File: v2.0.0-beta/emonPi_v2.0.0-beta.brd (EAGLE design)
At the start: 91.4 x 138.4 mm, 79 parts, among them IC1 AVR128DB32-I_PT, IC2 MCP1501-10E_SN, J1 SJ-3524-SMT-TR, J2 SJ-3524-SMT-TR, J4 SJ-3524-SMT-TR, J9 RJ11, Y1 MCSJK-7U-12.00-12-10-80-B-10

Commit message: updated board file
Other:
- board size 91.4 x 138.4 mm -> 85 x 88 mm

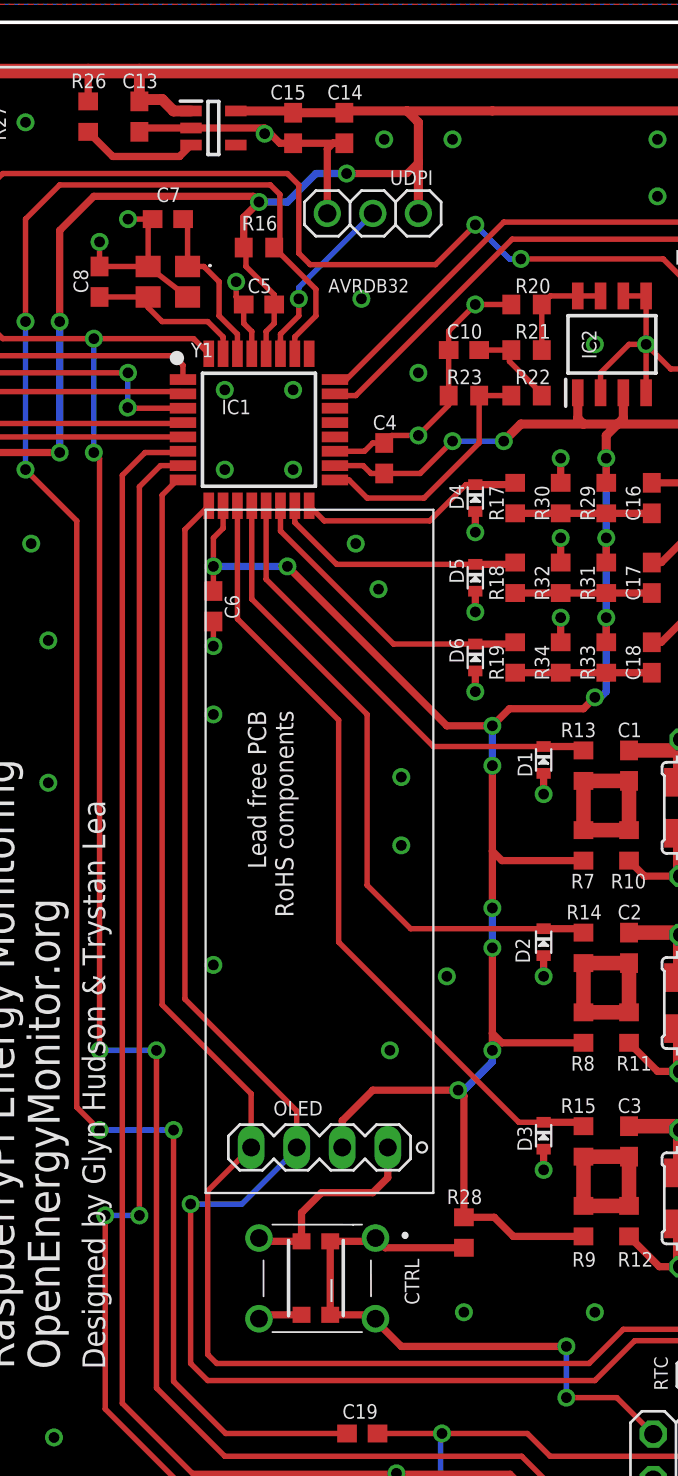
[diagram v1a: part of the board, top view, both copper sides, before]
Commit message: fix push switch
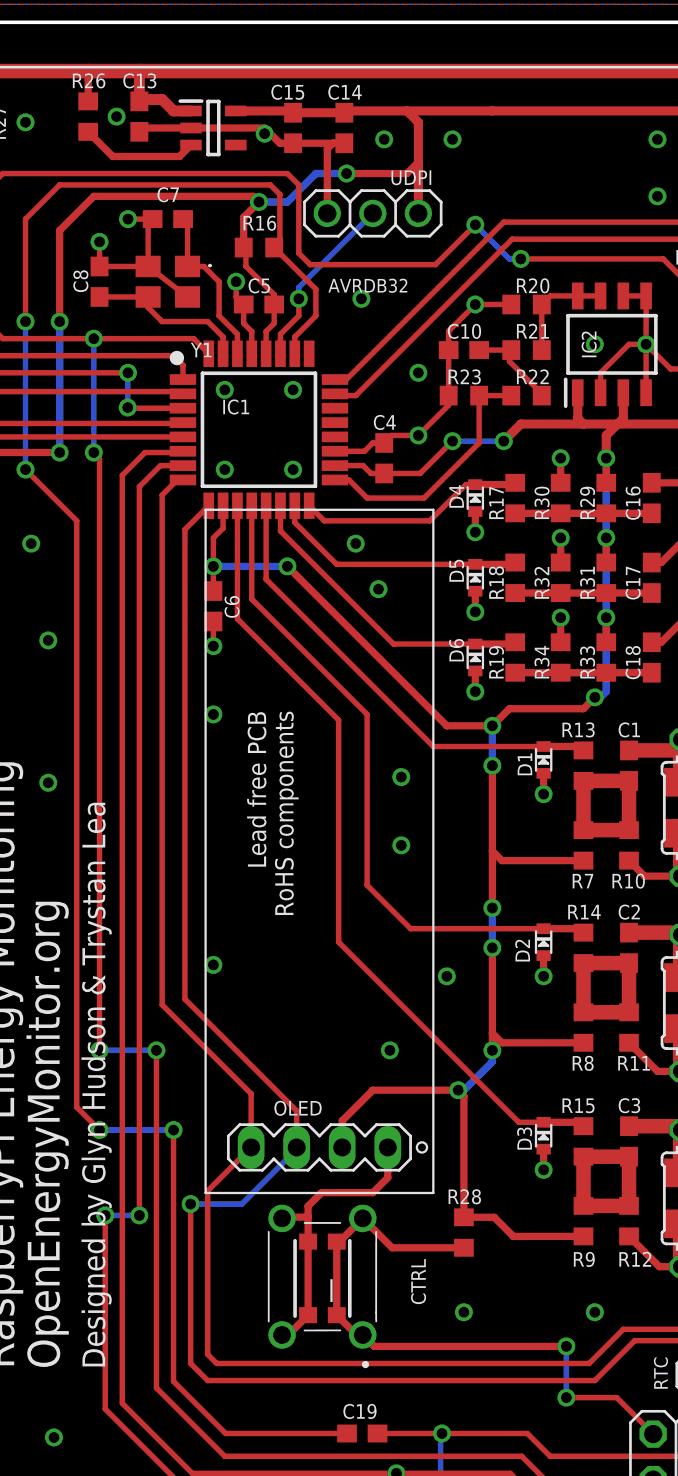
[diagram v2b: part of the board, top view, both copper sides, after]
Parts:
- moved S1 0.44 mm to (50.5, 15.6), turned to 270 degrees
- moved CTRL 0.37 mm to (50.5, 16.0)
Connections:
- net CONTROL: now also S1.3; no longer S1.2
- net GND: now also S1.2; no longer S1.3
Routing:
- net GND: track 185.2 -> 187.6 mm, vias 57 -> 58
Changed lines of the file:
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@@
 <attribute name="NAME" x="47.7455" y="25.033" size="0.8128" layer="25" font="vector" ratio="20"/>
 </element>
-<element name="CTRL" library="microbuilder" package="BTN_KMR2_4.6X2.8" value="KMR2" x="50.1175" y="15.97" smashed="yes" rot="R270">
-<attribute name="NAME" x="55.0705" y="17.0495" size="0.8128" layer="25" font="vector" ratio="20" rot="R270"/>
+<element name="CTRL" library="microbuilder" package="BTN_KMR2_4.6X2.8" value="KMR2" x="50.4825" y="15.9512" smashed="yes" rot="R270">
+<attribute name="NAME" x="55.4355" y="17.0307" size="0.8128" layer="25" font="vector" ratio="20" rot="R270"/>
 </element>
 <element name="R28" library="rcl" package="R0603" value="10K" x="58.3725" y="18.51" smashed="yes" rot="R270">
@@
 <attribute name="VALUE" x="82.9" y="10.445" size="1.27" layer="27" rot="R180"/>
 </element>
-<element name="S1" library="2-1825910-7" package="218259107" value="2-1825910-7" x="50.6825" y="15.9525" smashed="yes">
-<attribute name="ARROW_PART_NUMBER" value="2-1825910-7" x="50.6825" y="15.9525" size="0.8128" layer="27" font="vector" ratio="20" display="off"/>
-<attribute name="ARROW_PRICE-STOCK" value="https://www.arrow.com/en/products/2-1825910-7/te-connectivity?region=europe" x="50.6825" y="15.9525" size="0.8128" layer="27" font="vector" ratio="20" display="off"/>
-<attribute name="DESCRIPTION" value="Relays, Contactors &amp; Switches   Switches   Tactile Switches FSM14JH=6MM TACT SWITCH, HIGH TEMP" x="50.6825" y="15.9525" size="0.8128" layer="27" font="vector" ratio="20" display="off"/>
-<attribute name="HEIGHT" value="13mm" x="50.6825" y="15.9525" size="0.8128" layer="27" font="vector" ratio="20" display="off"/>
-<attribute name="MANUFACTURER_NAME" value="TE Connectivity" x="50.6825" y="15.9525" size="0.8128" layer="27" font="vector" ratio="20" display="off"/>
-<attribute name="MANUFACTURER_PART_NUMBER" value="2-1825910-7" x="50.6825" y="15.9525" size="0.8128" layer="27" font="vector" ratio="20" display="off"/>
-<attribute name="MOUSER_PART_NUMBER" value="506-2-1825910-7" x="50.6825" y="15.9525" size="0.8128" layer="27" font="vector" ratio="20" display="off"/>
-<attribute name="MOUSER_PRICE-STOCK" value="https://www.mouser.co.uk/ProductDetail/TE-Connectivity-PB/2-1825910-7?qs=epcAG6di8szpGFLvuwXKeQ%3D%3D" x="50.6825" y="15.9525" size="0.8128" layer="27" font="vector" ratio="20" display="off"/>
+<element name="S1" library="2-1825910-7" package="218259107" value="2-1825910-7" x="50.4825" y="15.5575" smashed="yes" rot="R270">
+<attribute name="ARROW_PART_NUMBER" value="2-1825910-7" x="50.4825" y="15.5575" size="0.8128" layer="27" font="vector" ratio="20" rot="R270" display="off"/>
+<attribute name="ARROW_PRICE-STOCK" value="https://www.arrow.com/en/products/2-1825910-7/te-connectivity?region=europe" x="50.4825" y="15.5575" size="0.8128" layer="27" font="vector" ratio="20" rot="R270" display="off"/>
+<attribute name="DESCRIPTION" value="Relays, Contactors &amp; Switches   Switches   Tactile Switches FSM14JH=6MM TACT SWITCH, HIGH TEMP" x="50.4825" y="15.5575" size="0.8128" layer="27" font="vector" ratio="20" rot="R270" display="off"/>
+<attribute name="HEIGHT" value="13mm" x="50.4825" y="15.5575" size="0.8128" layer="27" font="vector" ratio="20" rot="R270" display="off"/>
+<attribute name="MANUFACTURER_NAME" value="TE Connectivity" x="50.4825" y="15.5575" size="0.8128" layer="27" font="vector" ratio="20" rot="R270" display="off"/>
+<attribute name="MANUFACTURER_PART_NUMBER" value="2-1825910-7" x="50.4825" y="15.5575" size="0.8128" layer="27" font="vector" ratio="20" rot="R270" display="off"/>
+<attribute name="MOUSER_PART_NUMBER" value="506-2-1825910-7" x="50.4825" y="15.5575" size="0.8128" layer="27" font="vector" ratio="20" rot="R270" display="off"/>
+<attribute name="MOUSER_PRICE-STOCK" value="https://www.mouser.co.uk/ProductDetail/TE-Connectivity-PB/2-1825910-7?qs=epcAG6di8szpGFLvuwXKeQ%3D%3D" x="50.4825" y="15.5575" size="0.8128" layer="27" font="vector" ratio="20" rot="R270" display="off"/>
 </element>
 <element name="JP3" library="SparkFun" package="FTDI_BASIC" value="6x1" x="57.07" y="2.27" smashed="yes" rot="R180"/>
@@
 <vertex x="3" y="-4"/>
 </polygon>
-<contactref element="S1" pad="3"/>
-<contactref element="S1" pad="4"/>
-<wire x1="49.3175" y1="18.02" x2="47.125" y2="18.02" width="0.4064" layer="1"/>
-<wire x1="47.125" y1="18.02" x2="46.9425" y2="18.2025" width="0.4064" layer="1"/>
-<wire x1="49.3175" y1="13.92" x2="47.16" y2="13.92" width="0.4064" layer="1"/>
-<wire x1="47.16" y1="13.92" x2="46.9425" y2="13.7025" width="0.4064" layer="1"/>
-<wire x1="49.3175" y1="18.02" x2="49.3175" y2="19.615" width="0.4064" layer="1"/>
 <wire x1="54.1275" y1="21.5675" x2="54.1275" y2="23.255" width="0.4064" layer="1"/>
-<wire x1="49.3175" y1="19.615" x2="50.435" y2="20.7325" width="0.4064" layer="1"/>
 <wire x1="50.435" y1="20.7325" x2="53.2925" y2="20.7325" width="0.4064" layer="1"/>
 <wire x1="53.2925" y1="20.7325" x2="54.1275" y2="21.5675" width="0.4064" layer="1"/>
@@
 <contactref element="JP3" pad="GND"/>
 <contactref element="JP2" pad="5"/>
+<contactref element="S1" pad="4"/>
+<contactref element="S1" pad="2"/>
+<wire x1="49.6825" y1="18.0012" x2="49.6825" y2="19.3675" width="0.4064" layer="1"/>
+<wire x1="49.6825" y1="19.3675" x2="49.6825" y2="19.98" width="0.4064" layer="1"/>
+<wire x1="49.6825" y1="19.98" x2="50.435" y2="20.7325" width="0.4064" layer="1"/>
+<wire x1="48.2325" y1="19.2975" x2="48.3025" y2="19.3675" width="0.4064" layer="1"/>
+<wire x1="48.3025" y1="19.3675" x2="49.6825" y2="19.3675" width="0.4064" layer="1"/>
+<wire x1="48.2325" y1="12.7975" x2="48.5788" y2="12.7975" width="0.4064" layer="1"/>
+<wire x1="48.5788" y1="12.7975" x2="49.6825" y2="13.9012" width="0.4064" layer="1"/>
+<wire x1="49.6825" y1="18.0012" x2="49.6825" y2="13.9012" width="0.4064" layer="1"/>
+<via x="39.005" y="80.74" extent="1-16" drill="0.6"/>
 </signal>
 <signal name="3.3V">
@@
 <wire x1="66.8975" y1="9.3025" x2="64.0875" y2="9.3025" width="0.3048" layer="1"/>
 <contactref element="JP1" pad="11"/>
+<contactref element="S1" pad="3"/>
 <contactref element="S1" pad="1"/>
-<contactref element="S1" pad="2"/>
-<wire x1="50.9175" y1="18.02" x2="53.26" y2="18.02" width="0.4064" layer="1"/>
-<wire x1="53.26" y1="18.02" x2="53.4425" y2="18.2025" width="0.4064" layer="1"/>
-<wire x1="50.9175" y1="13.92" x2="53.225" y2="13.92" width="0.4064" layer="1"/>
-<wire x1="53.225" y1="13.92" x2="53.4425" y2="13.7025" width="0.4064" layer="1"/>
-<wire x1="53.4425" y1="18.2025" x2="53.985" y2="17.66" width="0.4064" layer="1"/>
-<wire x1="53.985" y1="17.66" x2="58.3725" y2="17.66" width="0.4064" layer="1"/>
-<wire x1="64.0875" y1="12.16" x2="54.88" y2="12.16" width="0.4064" layer="1"/>
-<wire x1="54.88" y1="12.16" x2="53.4425" y2="13.5975" width="0.4064" layer="1"/>
-<wire x1="53.4425" y1="13.5975" x2="53.4425" y2="13.7025" width="0.4064" layer="1"/>
-<wire x1="50.9175" y1="18.02" x2="50.9175" y2="13.92" width="0.4064" layer="1"/>
+<wire x1="52.7325" y1="19.2975" x2="51.4362" y2="18.0012" width="0.4064" layer="1"/>
+<wire x1="51.4362" y1="18.0012" x2="51.2825" y2="18.0012" width="0.4064" layer="1"/>
+<wire x1="58.3725" y1="17.66" x2="54.37" y2="17.66" width="0.4064" layer="1"/>
+<wire x1="54.37" y1="17.66" x2="52.7325" y2="19.2975" width="0.4064" layer="1"/>
+<wire x1="51.2825" y1="18.0012" x2="51.2825" y2="13.9012" width="0.4064" layer="1"/>
+<wire x1="51.2825" y1="13.9012" x2="52.3862" y2="12.7975" width="0.4064" layer="1"/>
+<wire x1="52.3862" y1="12.7975" x2="52.7325" y2="12.7975" width="0.4064" layer="1"/>
+<wire x1="52.7325" y1="12.7975" x2="53.37" y2="12.16" width="0.4064" layer="1"/>
+<wire x1="53.37" y1="12.16" x2="64.0875" y2="12.16" width="0.4064" layer="1"/>
 </signal>
 <signal name="N$16">
